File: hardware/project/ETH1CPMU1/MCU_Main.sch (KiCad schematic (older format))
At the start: 32 parts, among them J301 Conn_02x01, J302 Conn_02x05, U301 24LC08B-E/MS, U302 STM32F765ZGT6, Y301 NX3225GD-8MHZ-STD-CRA-3

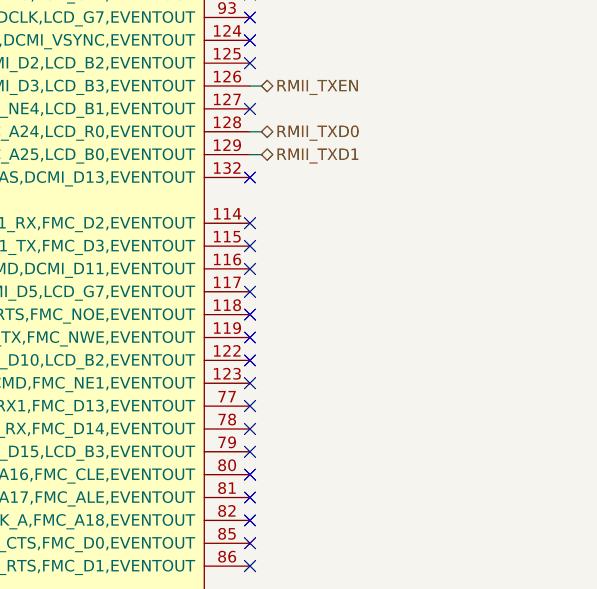
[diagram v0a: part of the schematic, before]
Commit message: Fixed problems with references to 3D models.
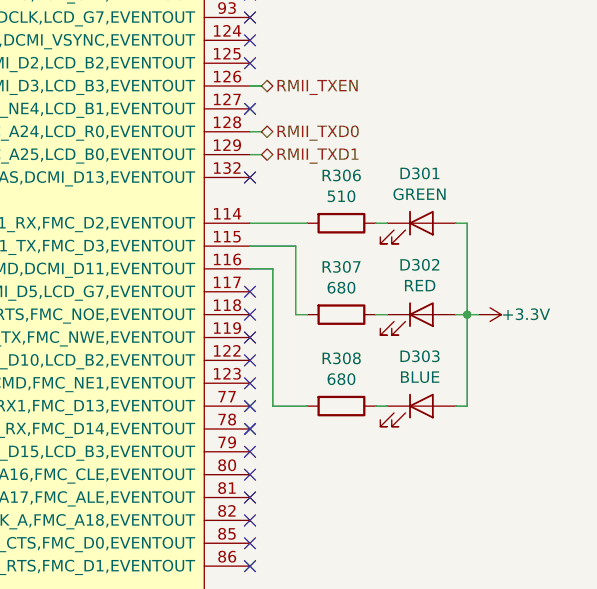
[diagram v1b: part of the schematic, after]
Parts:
- added D301: GREEN, LED_SMD:LED_0603_1608Metric_Pad1.05x0.95mm_HandSolder, symbol Device:LED
- added D302: RED, LED_SMD:LED_0603_1608Metric_Pad1.05x0.95mm_HandSolder, symbol Device:LED
- added D303: BLUE, LED_SMD:LED_0603_1608Metric_Pad1.05x0.95mm_HandSolder, symbol Device:LED
- added R306: 510, Resistor_SMD:R_0603_1608Metric_Pad1.05x0.95mm_HandSolder, symbol Device:R
- added R307, R308: 680, Resistor_SMD:R_0603_1608Metric_Pad1.05x0.95mm_HandSolder, symbol Device:R
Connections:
- net +3V3: now also D301.2 (A), D302.2 (A), D303.2 (A)
- net at U302.114 (PD0,DFSDM1_CKIN6,DFSDM1_DATIN7,UART4_RX,CAN1_RX,FMC_D2,EVENTOUT): now also R306.2
- net at U302.115 (PD1,DFSDM1_DATIN6,DFSDM1_CKIN7,UART4_TX,CAN1_TX,FMC_D3,EVENTOUT): now also R307.2
- net at U302.116 (PD2,TRACED2,TIM3_ETR,UART5_RX,SDMMC1_CMD,DCMI_D11,EVENTOUT): now also R308.2
- new net: D301.1 (K), R306.1
- new net: D302.1 (K), R307.1
- new net: D303.1 (K), R308.1
- no-connect marks 87 -> 84
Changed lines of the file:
@@
 NoConn ~ 14600 2350
 NoConn ~ 14600 2650
-NoConn ~ 14600 2850
-NoConn ~ 14600 2950
-NoConn ~ 14600 3050
 NoConn ~ 14600 3150
 NoConn ~ 14600 3250
@@
 NoConn ~ 14600 7750
 NoConn ~ 3200 4350
+$Comp
+L Device:R R306
+U 1 1 5E1BAAD6
+P 15000 2850
+F 0 "R306" V 14793 2850 50  0000 C CNN
+F 1 "510" V 14884 2850 50  0000 C CNN
+F 2 "Resistor_SMD:R_0603_1608Metric_Pad1.05x0.95mm_HandSolder" V 14930 2850 50  0001 C CNN
+F 3 "~" H 15000 2850 50  0001 C CNN
+	1    15000 2850
+	0    1    1    0
+$EndComp
+$Comp
+L Device:R R307
+U 1 1 5E1BBE19
+P 15000 3250
+F 0 "R307" V 14793 3250 50  0000 C CNN
+F 1 "680" V 14884 3250 50  0000 C CNN
+F 2 "Resistor_SMD:R_0603_1608Metric_Pad1.05x0.95mm_HandSolder" V 14930 3250 50  0001 C CNN
+F 3 "~" H 15000 3250 50  0001 C CNN
+	1    15000 3250
+	0    1    1    0
+$EndComp
+$Comp
+L Device:R R308
+U 1 1 5E1BC1BC
+P 15000 3650
+F 0 "R308" V 14793 3650 50  0000 C CNN
+F 1 "680" V 14884 3650 50  0000 C CNN
+F 2 "Resistor_SMD:R_0603_1608Metric_Pad1.05x0.95mm_HandSolder" V 14930 3650 50  0001 C CNN
+F 3 "~" H 15000 3650 50  0001 C CNN
+	1    15000 3650
+	0    1    1    0
+$EndComp
+Wire Wire Line
+	14600 2850 14850 2850
+Wire Wire Line
+	14850 3250 14800 3250
+Wire Wire Line
+	14800 2950 14600 2950
+Wire Wire Line
+	14850 3650 14700 3650
+Wire Wire Line
+	14700 3050 14600 3050
+$Comp
+L Device:LED D301
+U 1 1 5E209B01
+P 15350 2850
+F 0 "D301" H 15343 3066 50  0000 C CNN
+F 1 "GREEN" H 15343 2975 50  0000 C CNN
+F 2 "LED_SMD:LED_0603_1608Metric_Pad1.05x0.95mm_HandSolder" H 15350 2850 50  0001 C CNN
+F 3 "~" H 15350 2850 50  0001 C CNN
+	1    15350 2850
+	1    0    0    -1
+$EndComp
+$Comp
+L Device:LED D302
+U 1 1 5E20A2B0
+P 15350 3250
+F 0 "D302" H 15343 3466 50  0000 C CNN
+F 1 "RED" H 15343 3375 50  0000 C CNN
+F 2 "LED_SMD:LED_0603_1608Metric_Pad1.05x0.95mm_HandSolder" H 15350 3250 50  0001 C CNN
+F 3 "~" H 15350 3250 50  0001 C CNN
+	1    15350 3250
+	1    0    0    -1
+$EndComp
+Wire Wire Line
+	14700 3050 14700 3650
+Wire Wire Line
+	14800 2950 14800 3250
+$Comp
+L Device:LED D303
+U 1 1 5E24016A
+P 15350 3650
+F 0 "D303" H 15343 3866 50  0000 C CNN
+F 1 "BLUE" H 15343 3775 50  0000 C CNN
+F 2 "LED_SMD:LED_0603_1608Metric_Pad1.05x0.95mm_HandSolder" H 15350 3650 50  0001 C CNN
+F 3 "~" H 15350 3650 50  0001 C CNN
+	1    15350 3650
+	1    0    0    -1
+$EndComp
+Wire Wire Line
+	15150 3250 15200 3250
+Wire Wire Line
+	15150 2850 15200 2850
+Wire Wire Line
+	15150 3650 15200 3650
+Wire Wire Line
+	15550 3650 15550 3250
+Wire Wire Line
+	15550 2850 15500 2850
+Wire Wire Line
+	15500 3650 15550 3650
+Wire Wire Line
+	15500 3250 15550 3250
+Connection ~ 15550 3250
+Wire Wire Line
+	15550 3250 15550 2850
+$Comp
+L power:+3.3V #PWR0325
+U 1 1 5E279CD6
+P 15600 3250
+F 0 "#PWR0325" H 15600 3100 50  0001 C CNN
+F 1 "+3.3V" V 15600 3350 50  0000 L CNN
+F 2 "" H 15600 3250 50  0001 C CNN
+F 3 "" H 15600 3250 50  0001 C CNN
+	1    15600 3250
+	0    1    1    0
+$EndComp
+Wire Wire Line
+	15600 3250 15550 3250
 $EndSCHEMATC
